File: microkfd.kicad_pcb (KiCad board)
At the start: 2 copper layers, 55 x 25.5 mm, 48 parts, among them J1 USB_B_Micro, J2 AudioJack3, J3 OLED, Q1 T2N7002, Q2 T2N7002, SW1 RST, SW2 DOWN, SW3 ENT, SW4 UP, U1 SP3003-02, U2 ATmega32U4RC-A, Y1 16MHz

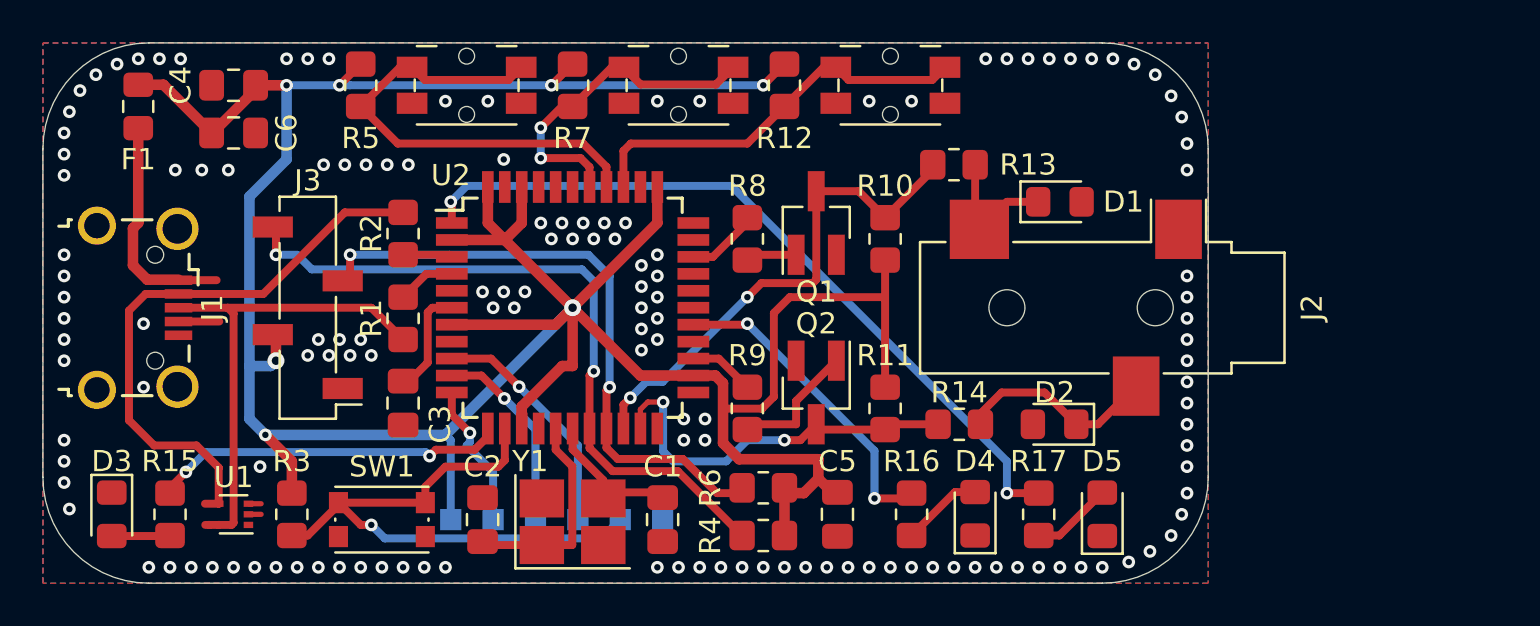
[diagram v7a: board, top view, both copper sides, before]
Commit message: revision E - atmega328p redesign
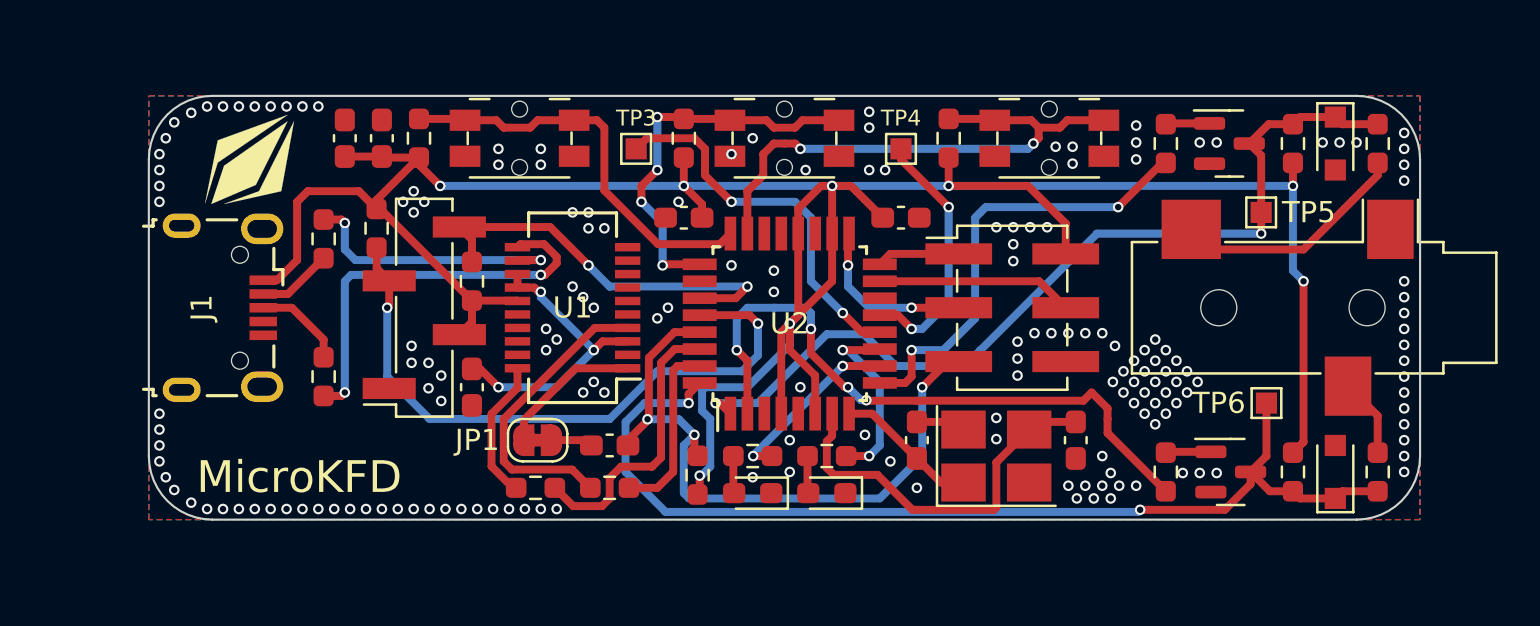
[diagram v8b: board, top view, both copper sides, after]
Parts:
- removed C1: 10pF, Capacitor_SMD:C_0805_2012Metric_Pad1.18x1.45mm_HandSolder
- removed C3: 1uF, Capacitor_SMD:C_0805_2012Metric_Pad1.18x1.45mm_HandSolder
- removed D5: ACT, Diode_SMD:D_0805_2012Metric_Pad1.15x1.40mm_HandSolder
- removed F1: 100mA, Fuse:Fuse_0805_2012Metric_Pad1.15x1.40mm_HandSolder
- removed SW4: UP, Button_Switch_SMD:Panasonic_EVQPUM_EVQPUD
- removed TP1: MOSI, TestPoint:TestPoint_Pad_1.0x1.0mm
- removed TP2: SCK, TestPoint:TestPoint_Pad_1.0x1.0mm
- added C10: 10pF, Capacitor_SMD:C_0603_1608Metric_Pad1.08x0.95mm_HandSolder, F.Cu at (138.8, 106.2)
- added C7: 0.1uF, Capacitor_SMD:C_0603_1608Metric_Pad1.08x0.95mm_HandSolder, F.Cu at (120.2, 95.8)
- added C8: 0.1uF, Capacitor_SMD:C_0603_1608Metric_Pad1.08x0.95mm_HandSolder, F.Cu at (130.5, 95.8)
- added C9: 10pF, Capacitor_SMD:C_0603_1608Metric_Pad1.08x0.95mm_HandSolder, F.Cu at (131.2, 106.2)
- added J4: AudioJack3, Connector_Audio:Jack_3.5mm_CUI_SJ-3523-SMT_Horizontal, F.Cu at (150.0, 100.0)
- added JP1: RST_EN, Jumper:SolderJumper-2_P1.3mm_Bridged_RoundedPad1.0x1.5mm, F.Cu at (113.3, 106.2)
- added R18: 220, Resistor_SMD:R_0603_1608Metric_Pad0.98x0.95mm_HandSolder, F.Cu at (153.0, 107.8)
- C2: value 10pF -> 0.1uF; footprint Capacitor_SMD:C_0805_2012Metric_Pad1.18x1.45mm_HandSolder -> Capacitor_SMD:C_0603_1608Metric_Pad1.08x0.95mm_HandSolder
- C4: value 1uF -> 10uF; footprint Capacitor_SMD:C_0805_2012Metric_Pad1.18x1.45mm_HandSolder -> Capacitor_SMD:C_0603_1608Metric_Pad1.08x0.95mm_HandSolder
- C5, C6: footprint Capacitor_SMD:C_0805_2012Metric_Pad1.18x1.45mm_HandSolder -> Capacitor_SMD:C_0603_1608Metric_Pad1.08x0.95mm_HandSolder
- D1: value 9V6 -> D_SNS; footprint Diode_SMD:D_0805_2012Metric_Pad1.15x1.40mm_HandSolder -> LED_SMD:LED_0603_1608Metric_Pad1.05x0.95mm_HandSolder
- D2: value 9V6 -> D_ACT; footprint Diode_SMD:D_0805_2012Metric_Pad1.15x1.40mm_HandSolder -> LED_SMD:LED_0603_1608Metric_Pad1.05x0.95mm_HandSolder
- D3: value PWR -> 6.3V; footprint Diode_SMD:D_0805_2012Metric_Pad1.15x1.40mm_HandSolder -> Diode_SMD:D_SOD-323_HandSoldering
- D4: value SNS -> 6.3V; footprint Diode_SMD:D_0805_2012Metric_Pad1.15x1.40mm_HandSolder -> Diode_SMD:D_SOD-323_HandSoldering
- G***: moved to F.Cu
- J1: footprint Connector_USB:USB_Micro-B_Wuerth_629105150521_CircularHoles -> Connector_USB:USB_Micro-B_Wuerth_629105150521
- J2: value AudioJack3 -> AVR-ISP-6; footprint Connector_Audio:Jack_3.5mm_CUI_SJ-3523-SMT_Horizontal -> Connector_PinHeader_2.54mm:PinHeader_2x03_P2.54mm_Vertical_SMD
- J3: footprint Connector_PinSocket_2.54mm:PinSocket_1x04_P2.54mm_Vertical_SMD_Pin1Left -> Connector_PinHeader_2.54mm:PinHeader_1x04_P2.54mm_Vertical_SMD_Pin1Right
- Q1, Q2: value T2N7002 -> MMBT3904; footprint Package_TO_SOT_SMD:SOT-23_Handsoldering -> Package_TO_SOT_SMD:SOT-23
- R1, R10, R11, R2, R3, R5: footprint Resistor_SMD:R_0805_2012Metric_Pad1.20x1.40mm_HandSolder -> Resistor_SMD:R_0603_1608Metric_Pad0.98x0.95mm_HandSolder
- R12, R7, R8, R9: value 10k -> 1k; footprint Resistor_SMD:R_0805_2012Metric_Pad1.20x1.40mm_HandSolder -> Resistor_SMD:R_0603_1608Metric_Pad0.98x0.95mm_HandSolder
- R13: value 220 -> 1k; footprint Resistor_SMD:R_0805_2012Metric_Pad1.20x1.40mm_HandSolder -> Resistor_SMD:R_0603_1608Metric_Pad0.98x0.95mm_HandSolder
- R14: value 220 -> 10k; footprint Resistor_SMD:R_0805_2012Metric_Pad1.20x1.40mm_HandSolder -> Resistor_SMD:R_0603_1608Metric_Pad0.98x0.95mm_HandSolder
- R15, R16: value 1k -> 10k; footprint Resistor_SMD:R_0805_2012Metric_Pad1.20x1.40mm_HandSolder -> Resistor_SMD:R_0603_1608Metric_Pad0.98x0.95mm_HandSolder
- R17: value 1k -> 220; footprint Resistor_SMD:R_0805_2012Metric_Pad1.20x1.40mm_HandSolder -> Resistor_SMD:R_0603_1608Metric_Pad0.98x0.95mm_HandSolder
- R4: value 4k7 -> 10k; footprint Resistor_SMD:R_0805_2012Metric_Pad1.20x1.40mm_HandSolder -> Resistor_SMD:R_0603_1608Metric_Pad0.98x0.95mm_HandSolder
- R6: value 4k7 -> 1k; footprint Resistor_SMD:R_0805_2012Metric_Pad1.20x1.40mm_HandSolder -> Resistor_SMD:R_0603_1608Metric_Pad0.98x0.95mm_HandSolder
- SW1: value RST -> SW_UP; footprint Button_Switch_SMD:SW_Push_1P1T_NO_CK_KMR2 -> Button_Switch_SMD:Panasonic_EVQPUM_EVQPUD
- SW2: value DOWN -> SW_DN
- SW3: value ENT -> SW_ENT
- TP3: value MISO -> GPIO1; moved to F.Cu
- TP4: value RST -> GPIO2; moved to F.Cu
- TP5: value VCC -> KFD_DATA; moved to F.Cu
- TP6: value GND -> KFD_SENSE; moved to F.Cu
- U1: value SP3003-02 -> FT231XS; footprint Package_TO_SOT_SMD:SOT-553 -> Package_SO:SSOP-20_3.9x8.7mm_P0.635mm
- U2: value ATmega32U4RC-A -> ATmega328P-A; footprint Package_QFP:TQFP-44_10x10mm_P0.8mm -> Package_QFP:TQFP-32_7x7mm_P0.8mm
- Y1: footprint Crystal:Crystal_SMD_SeikoEpson_FA238-4Pin_3.2x2.5mm_HandSoldering -> Crystal:Crystal_SMD_SeikoEpson_FA238V-4Pin_3.2x2.5mm_HandSoldering
- moved D3 60.3 mm to (151.0, 92.2)
- moved R15 53.0 mm to (149.0, 107.8), turned to 90 degrees
- moved TP5 40.9 mm to (147.5, 95.5)
- moved G*** 38.0 mm to (99.8, 93.0), turned to 0 degrees
- moved SW1 36.3 mm to (137.5, 92.0), turned to 0 degrees
- moved TP6 29.0 mm to (147.8, 104.5)
- moved R11 25.4 mm to (107.8, 92.0), turned to -90 degrees
- moved R17 23.7 mm to (153.0, 92.2), turned to 90 degrees
- moved C6 23.1 mm to (116.8, 106.5)
- moved TP4 22.0 mm to (130.5, 92.5)
- moved R16 20.8 mm to (120.2, 92.0)
- moved R14 20.6 mm to (149.0, 92.2), turned to -90 degrees
- moved Y1 20.2 mm to (135.0, 107.0)
- moved D1 20.0 mm to (123.5, 108.8), turned to 180 degrees
- moved Q2 19.9 mm to (146.1, 107.8), turned to 0 degrees
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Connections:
- C2 pad 1: GND -> +5V
- C2 pad 2: XT2 -> GND
- C4 pad 1: GND -> +5V
- C4 pad 2: +5V -> GND
- C5 pad 1: GND -> Net-(C5-Pad1)
- C5 pad 2: +5V -> GND
- C6 pad 1: +5V -> Net-(C6-Pad1)
- C6 pad 2: GND -> ~{RESET}
- D1 pad 1: Net-(D1-Pad1) -> GND
- D1 pad 2: GND -> Net-(D1-Pad2)
- D2 pad 1: Net-(D2-Pad1) -> GND
- D2 pad 2: GND -> Net-(D2-Pad2)
- D3 pad 1: GND -> TWI_D_RX
- D3 pad 2: Net-(D3-Pad2) -> GND
- D4 pad 1: GND -> TWI_S_RX
- D4 pad 2: Net-(D4-Pad2) -> GND
- J1 pad 1: Net-(F1-Pad2) -> +5V
- J3 pad 3: I2C_SDA -> SCL
- J3 pad 4: I2C_SCL -> SDA
- Q1 pad 3: DATA_IN -> TWI_D_RX
- Q2 pad 3: SENSE_IN -> TWI_S_RX
- R1 pad 1: Net-(R1-Pad1) -> Net-(J1-Pad2)
- R1 pad 2: Net-(J1-Pad3) -> Net-(R1-Pad2)
- R10 pad 1: DATA_IN -> A0
- R11 pad 1: SENSE_IN -> A1
- R12 pad 1: SW_UP -> Net-(Q1-Pad1)
- R12 pad 2: +5V -> TWI_D_TX
- R13 pad 1: DATA_IN -> Net-(Q2-Pad1)
- R13 pad 2: Net-(D1-Pad1) -> TWI_S_TX
- R14 pad 1: SENSE_IN -> TWI_D_RX
- R14 pad 2: Net-(D2-Pad1) -> +5V
- R15 pad 1: LED_PWR -> TWI_S_RX
- R15 pad 2: Net-(D3-Pad2) -> +5V
- R16 pad 1: LED_SNS -> A2
- R16 pad 2: Net-(D4-Pad2) -> +5V
- R17 pad 1: LED_ACT -> KFD_DATA
- R17 pad 2: Net-(D5-Pad2) -> TWI_D_RX
- R2 pad 1: Net-(J1-Pad2) -> Net-(J1-Pad3)
- R3 pad 1: RST -> ~{RESET}
- R4 pad 1: I2C_SCL -> SDA
- R5 pad 1: SW_DN -> SCL
- R6 pad 1: I2C_SDA -> S_TX
- R6 pad 2: +5V -> Net-(R6-Pad2)
- R7 pad 1: SW_ENT -> S_RX
- R7 pad 2: +5V -> Net-(R7-Pad2)
- R8 pad 1: Net-(Q1-Pad1) -> Net-(D1-Pad2)
- R8 pad 2: DATA_OUT -> Net-(R8-Pad2)
- R9 pad 1: Net-(Q2-Pad1) -> Net-(D2-Pad2)
- R9 pad 2: SENSE_OUT -> Net-(R9-Pad2)
- SW1 pad 1: GND -> A0
- SW1 pad 2: RST -> GND
- SW2 pad 1: SW_DN -> A1
- SW3 pad 1: SW_ENT -> A2
- TP3 pad 1: MISO -> GPIO1
- TP4 pad 1: RST -> GPIO2
- TP5 pad 1: +5V -> TWI_D_RX
- TP6 pad 1: GND -> TWI_S_RX
- U1 pad 1: (no net) -> Net-(JP1-Pad1)
- U1 pad 2: GND -> unconnected-(U1-Pad2)
- U1 pad 3: unconnected-(U1-Pad3) -> Net-(C5-Pad1)
- U1 pad 4: Net-(J1-Pad2) -> S_RX
- U1 pad 5: Net-(J1-Pad3) -> unconnected-(U1-Pad5)
- U2 pad 1: LED_ACT -> TWI_D_RX
- U2 pad 10: MOSI -> Net-(R8-Pad2)
- U2 pad 11: MISO -> Net-(R9-Pad2)
- U2 pad 12: LED_PWR -> GPIO1
- U2 pad 13: RST -> GPIO2
- U2 pad 14: +5V -> unconnected-(U2-Pad14)
- U2 pad 15: GND -> MOSI
- U2 pad 16: XT2 -> MISO
- U2 pad 17: XT1 -> SCK
- U2 pad 18: I2C_SCL -> +5V
- U2 pad 19: I2C_SDA -> unconnected-(U2-Pad19)
- U2 pad 2: +5V -> TWI_S_TX
- U2 pad 20: DATA_IN -> +5V
- U2 pad 21: SENSE_IN -> GND
- U2 pad 23: GND -> A0
- U2 pad 24: +5V -> A1
- U2 pad 25: SENSE_OUT -> A2
- U2 pad 27: LED_SNS -> SDA
- U2 pad 28: unconnected-(U2-Pad28) -> SCL
- U2 pad 29: unconnected-(U2-Pad29) -> ~{RESET}
- U2 pad 3: Net-(R2-Pad2) -> GND
- U2 pad 30: unconnected-(U2-Pad30) -> Net-(R6-Pad2)
- U2 pad 31: DATA_OUT -> Net-(R7-Pad2)
- U2 pad 32: unconnected-(U2-Pad32) -> TWI_S_RX
- U2 pad 4: Net-(R1-Pad1) -> +5V
- U2 pad 6: Net-(C3-Pad1) -> +5V
- U2 pad 7: +5V -> Net-(C10-Pad2)
- U2 pad 8: unconnected-(U2-Pad8) -> Net-(C9-Pad2)
- U2 pad 9: SCK -> TWI_D_TX
- Y1 pad 1: XT2 -> Net-(C9-Pad2)
- Y1 pad 3: XT1 -> Net-(C10-Pad2)
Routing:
- net TWI_S_RX: track 0.00 -> 48.5 mm, vias 0 -> 2
- net TWI_D_RX: track 0.00 -> 42.4 mm, vias 0 -> 2
- net LED_ACT: track 36.0 -> 0.00 mm, vias 2 -> 0
- net I2C_SCL: track 33.8 -> 0.00 mm, vias 2 -> 0
- net TWI_S_TX: track 0.00 -> 30.9 mm, vias 0 -> 4
- net ~{RESET}: track 0.00 -> 30.8 mm, vias 0 -> 3
- net SCL: track 0.00 -> 30.4 mm, vias 0 -> 2
- net I2C_SDA: track 29.5 -> 0.00 mm, vias 2 -> 0
- net RST: track 27.9 -> 0.00 mm, vias 1 -> 0
- net A0: track 0.00 -> 25.7 mm, vias 0 -> 2
- net DATA_IN: track 24.0 -> 0.00 mm, vias 2 -> 0
- net Net-(J1-Pad2): track 27.5 -> 3.55 mm
- net SW_DN: track 22.6 -> 0.00 mm
- net TWI_D_TX: track 0.00 -> 21.3 mm, vias 0 -> 2
- net +5V: track 154.1 -> 133.0 mm, vias 7 -> 8
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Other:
- board size 55 x 25.5 mm -> 60 x 20 mm
- board text added: "rev E - 01/23"
- board text removed: "5V"
- board text removed: "GND"
- board text removed: "MISO"
- board text removed: "MOSI"
- board text removed: "RST"
- board text removed: "SCK"
- board text removed: "rev D 2022-04-09"
